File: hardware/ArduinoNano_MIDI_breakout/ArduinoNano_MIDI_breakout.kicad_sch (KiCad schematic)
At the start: 32 parts, among them J2 MIDI OUT, J3 MIDI IN, J4 I2C, Q1 2N3904, SW1 RotaryEncoder_Switch, SW2 SW_Push, SW3 SW_Push, SW4 SW_DPDT_x2, U2 6N139

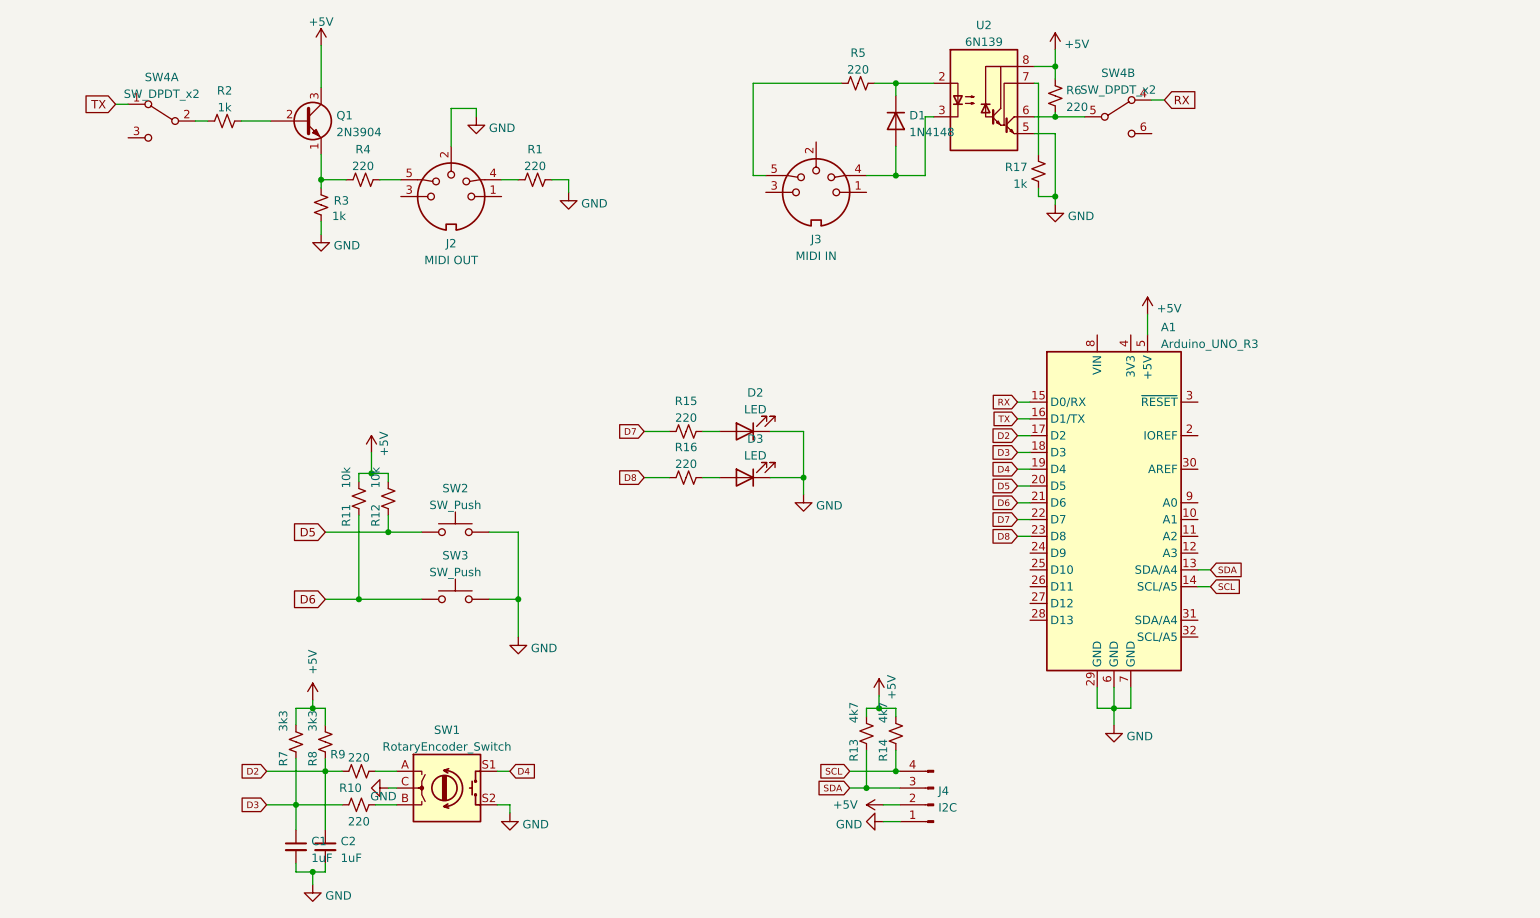
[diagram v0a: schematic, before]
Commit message: MIDI Breakout Variations
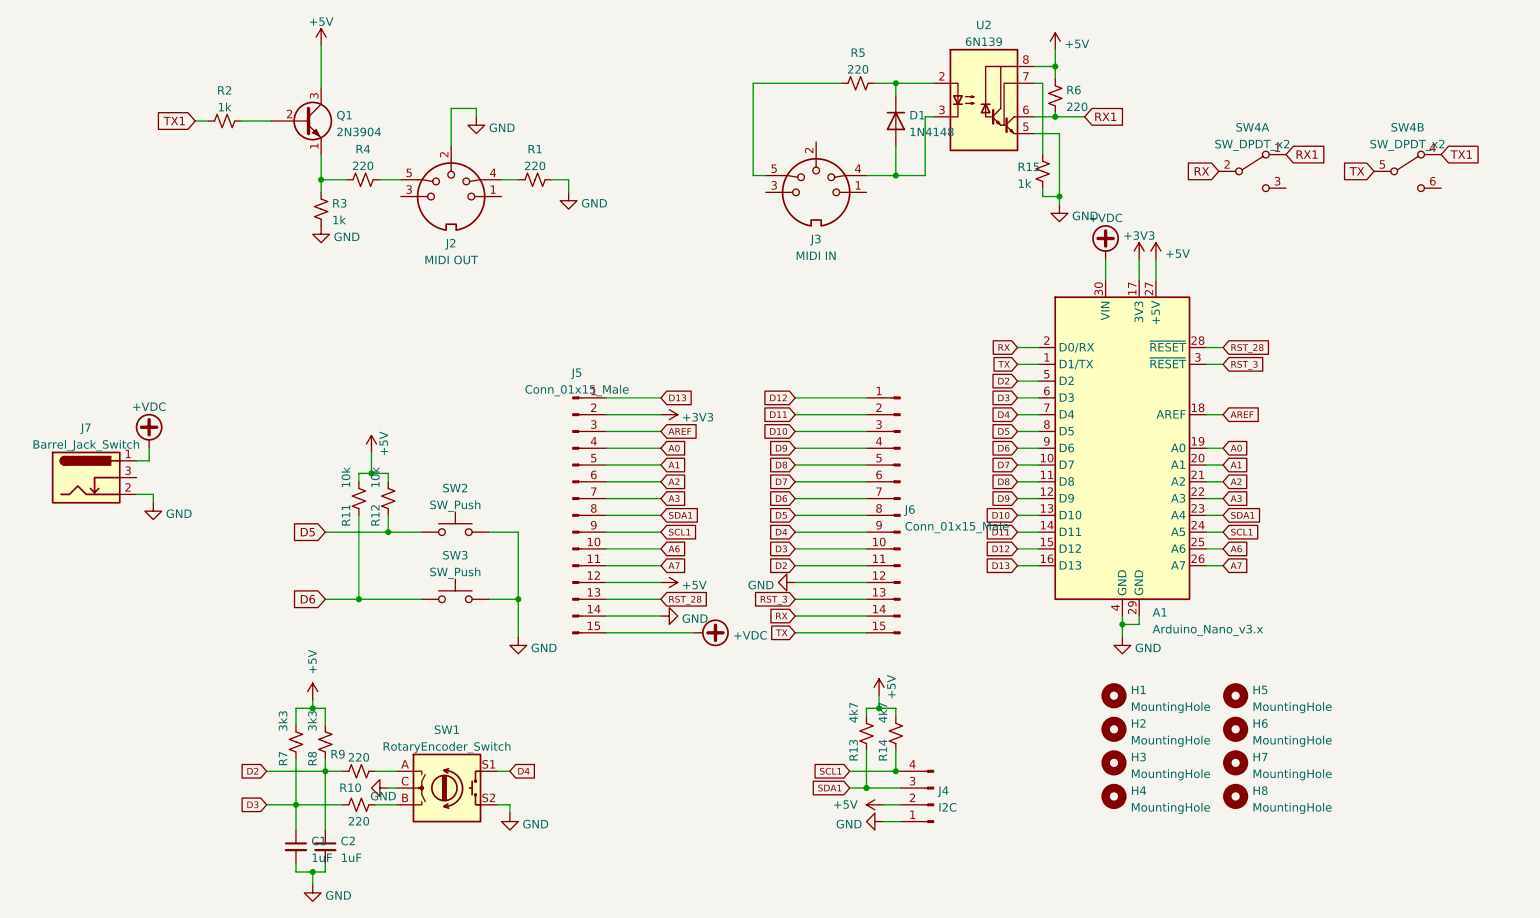
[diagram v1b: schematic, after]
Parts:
- removed A1: Arduino_UNO_R3, Module:Arduino_UNO_R3, symbol MCU_Module:Arduino_UNO_R3
- removed D2, D3: LED, LED_THT:LED_D5.0mm, symbol Device:LED
- removed R16: 220, Resistor_THT:R_Axial_DIN0207_L6.3mm_D2.5mm_P7.62mm_Horizontal, symbol Device:R_Small_US
- removed R17: 1k, Resistor_THT:R_Axial_DIN0207_L6.3mm_D2.5mm_P7.62mm_Horizontal, symbol Device:R_Small_US
- added A1: Arduino_Nano_v3.x, Module:Arduino_Nano, symbol MCU_Module:Arduino_Nano_v3.x
- added H1, H2, H3, H4, H5, H6, H7, H8: MountingHole, MountingHole:MountingHole_3.2mm_M3_DIN965_Pad, symbol Mechanical:MountingHole
- added J5, J6: Conn_01x15_Male, Connector_PinHeader_2.54mm:PinHeader_1x15_P2.54mm_Vertical, symbol Connector:Conn_01x15_Male
- added J7: Barrel_Jack_Switch, Connector_BarrelJack:BarrelJack_GCT_DCJ200-10-A_Horizontal, symbol Connector:Barrel_Jack_Switch
- R15: value 220 -> 1k
- SW4: footprint Button_Switch_THT:SW_CuK_JS202011CQN_DPDT_Straight -> Button_Switch_THT:SW_E-Switch_EG1271_DPDT
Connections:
- net +5V: now also A1.27 (+5V), J5.12 (Pin_12)
- net D2: now also A1.5 (D2), J6.11 (Pin_11)
- net D3: now also A1.6 (D3), J6.10 (Pin_10)
- net D4: now also A1.7 (D4), J6.9 (Pin_9)
- net D5: now also A1.8 (D5), J6.8 (Pin_8)
- net D6: now also A1.9 (D6), J6.7 (Pin_7)
- net D7: now also A1.10 (D7), J6.6 (Pin_6); no longer R15.1
- net D8: now also A1.11 (D8), J6.5 (Pin_5)
- net GND: now also R15.2, A1.29 (GND), A1.4 (GND), J5.14 (Pin_14), J6.12 (Pin_12), J7.2
- net RX: now also SW4.2 (B), A1.2 (D0/RX), J6.14 (Pin_14); no longer SW4.4 (A)
- net TX: now also SW4.5 (B), A1.1 (D1/TX), J6.15 (Pin_15); no longer SW4.1 (A)
- net RX1: now reaches R6.1, U2.6 (VO2)
- net RX1: now also SW4.1 (A); no longer SW4.5 (B)
- net at U2.7 (VO1): now also R15.1
- net TX1: now reaches R2.1
- net TX1: now also SW4.4 (A); no longer SW4.2 (B)
- net SCL renamed SCL1
- net SCL1: now also A1.24 (A5), J5.9 (Pin_9)
- net SDA renamed SDA1
- net SDA1: now also A1.23 (A4), J5.8 (Pin_8)
- new net +3V3: A1.17 (3V3), J5.2 (Pin_2)
- new net +VDC: A1.30 (VIN), J5.15 (Pin_15), J7.1
- new net A0: A1.19 (A0), J5.4 (Pin_4)
- new net A1: A1.20 (A1), J5.5 (Pin_5)
- new net A2: A1.21 (A2), J5.6 (Pin_6)
- new net A3: A1.22 (A3), J5.7 (Pin_7)
- new net A6: A1.25 (A6), J5.10 (Pin_10)
- new net A7: A1.26 (A7), J5.11 (Pin_11)
- new net AREF: A1.18 (AREF), J5.3 (Pin_3)
- new net D10: A1.13 (D10), J6.3 (Pin_3)
- new net D11: A1.14 (D11), J6.2 (Pin_2)
- new net D12: A1.15 (D12), J6.1 (Pin_1)
- new net D13: A1.16 (D13), J5.1 (Pin_1)
- new net D9: A1.12 (D9), J6.4 (Pin_4)
- new net RST_28: A1.28 (~{RESET}), J5.13 (Pin_13)
- new net RST_3: A1.3 (~{RESET}), J6.13 (Pin_13)
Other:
- moved on the sheet: R3

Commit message: Fixed MIDI pinout swap
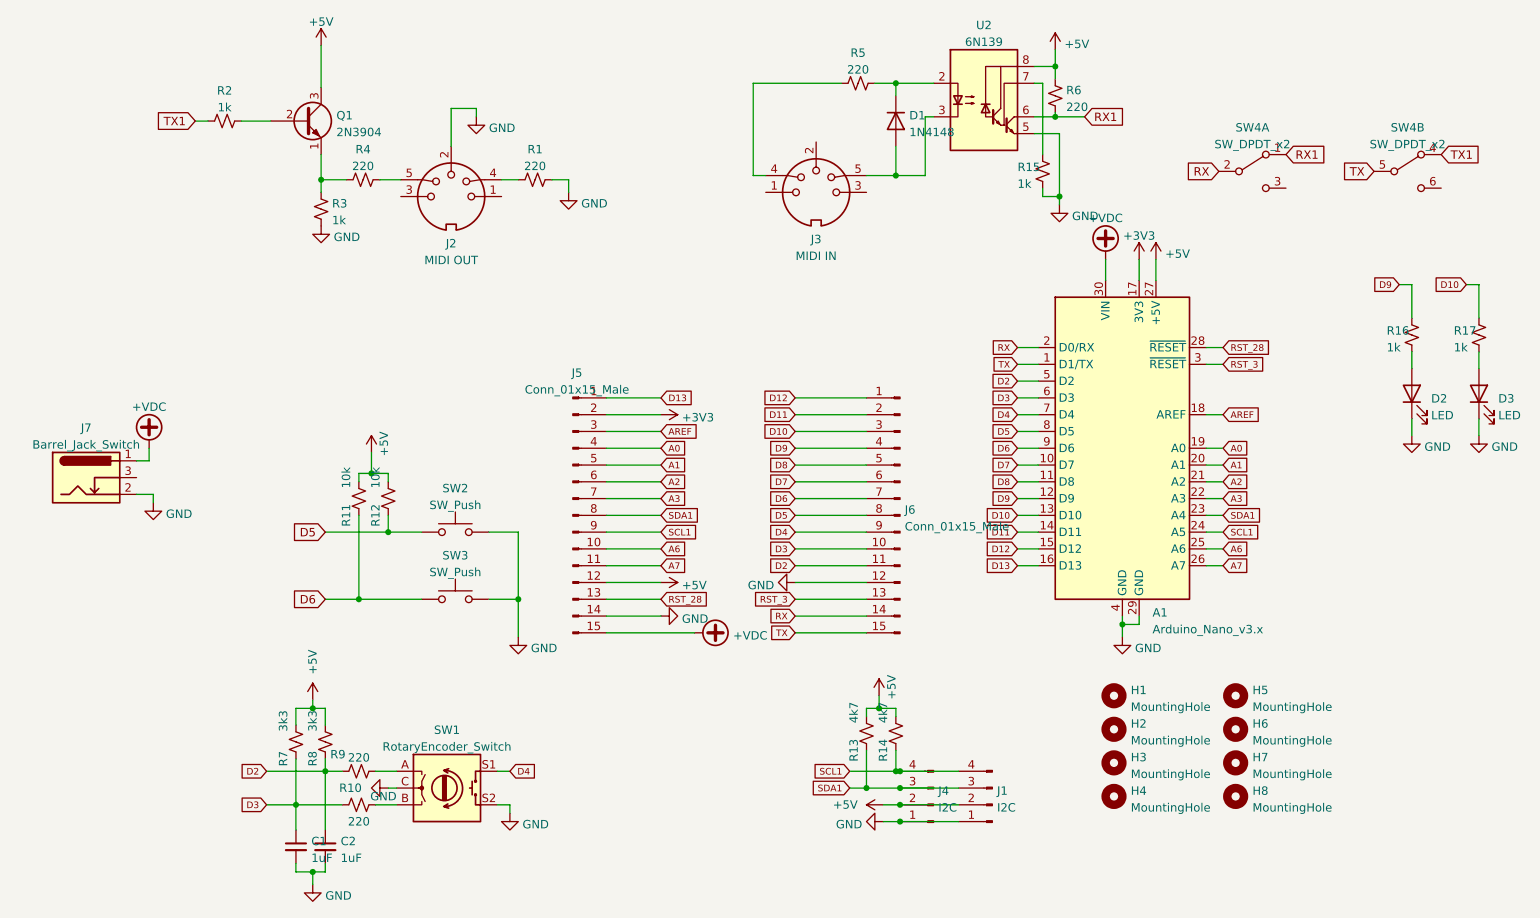
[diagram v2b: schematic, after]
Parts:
- added D2, D3: LED, LED_THT:LED_D5.0mm, symbol Device:LED
- added J1: I2C, Connector_PinHeader_2.54mm:PinHeader_1x04_P2.54mm_Vertical, symbol Connector:Conn_01x04_Male
- added R16, R17: 1k, Resistor_THT:R_Axial_DIN0207_L6.3mm_D2.5mm_P7.62mm_Horizontal, symbol Device:R_Small_US
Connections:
- net +5V: now also J1.2 (Pin_2)
- net D10: now also R17.1
- net D9: now also R16.1
- net GND: now also D2.1 (K), D3.1 (K), J1.1 (Pin_1)
- net SCL1: now also J1.4 (Pin_4)
- net SDA1: now also J1.3 (Pin_3)
- net at R5.1: now also J3.4; no longer J3.5
- net at D1.2 (A), U2.3 (C2): now also J3.5; no longer J3.4
- new net: D2.2 (A), R16.2
- new net: D3.2 (A), R17.2

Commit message: Fixes to Nano Breakout
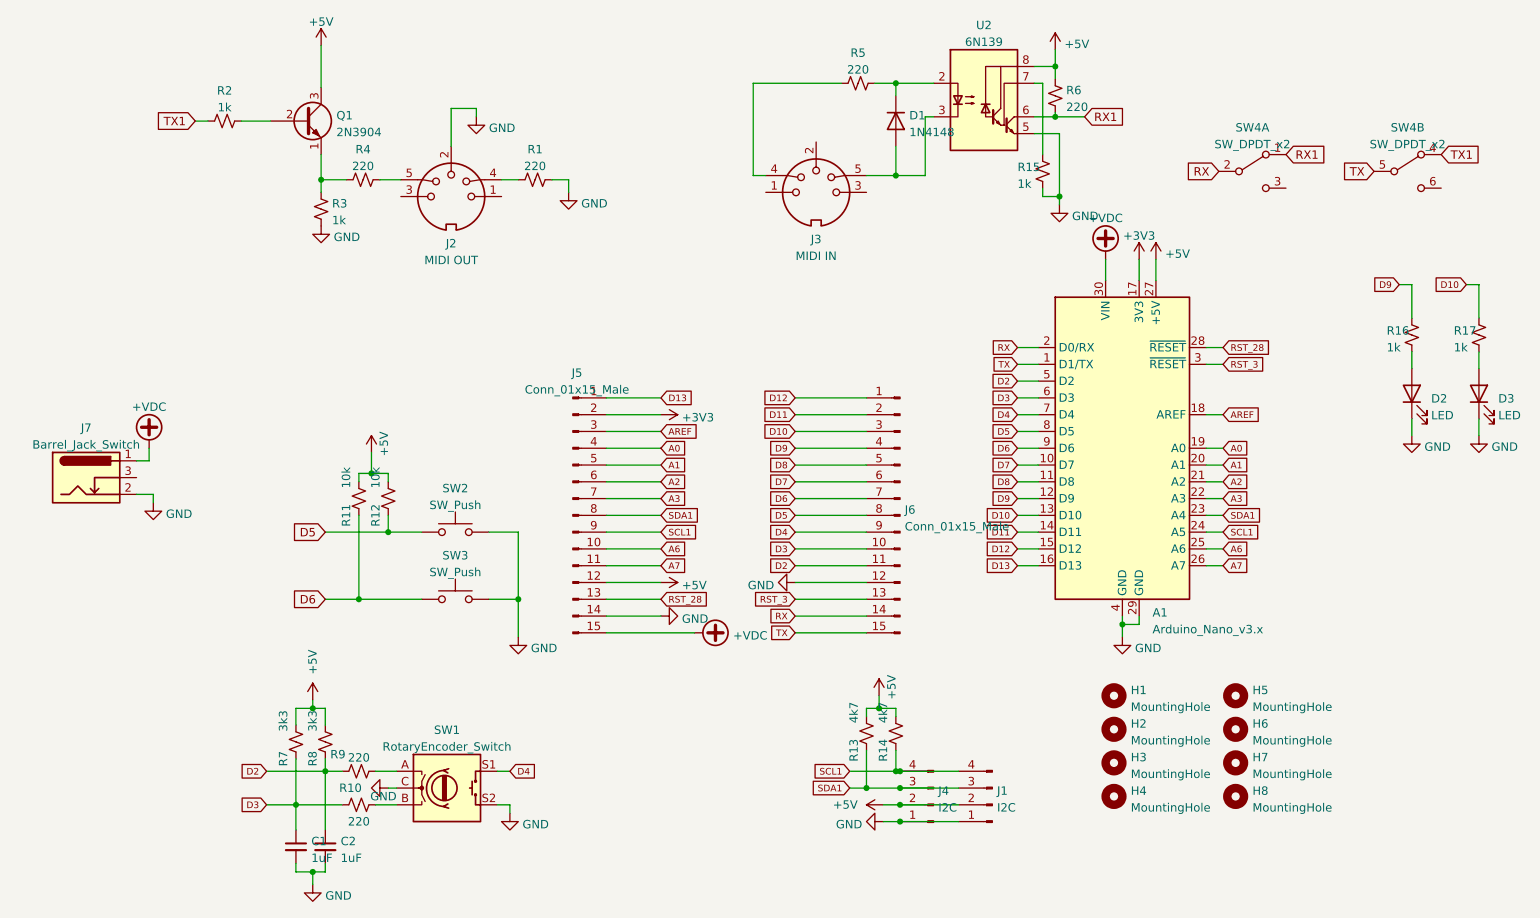
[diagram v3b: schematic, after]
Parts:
- SW4: footprint Button_Switch_THT:SW_E-Switch_EG1271_DPDT -> Button_Switch_THT:SW_CuK_JS202011CQN_DPDT_Straight
